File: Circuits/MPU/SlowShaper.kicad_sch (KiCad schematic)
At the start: 34 parts, among them U22 ADA4805-2ARMZ, U23 ADA4805-2ARMZ

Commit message: revert cap changes from sim. Don't trust it...
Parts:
- C98: value 3.9nF -> 3.3nF
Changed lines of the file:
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@@
 			)
 		)
-		(property "Value" "3.9nF"
+		(property "Value" "3.3nF"
 			(at 149.86 102.87 90)
 			(effects

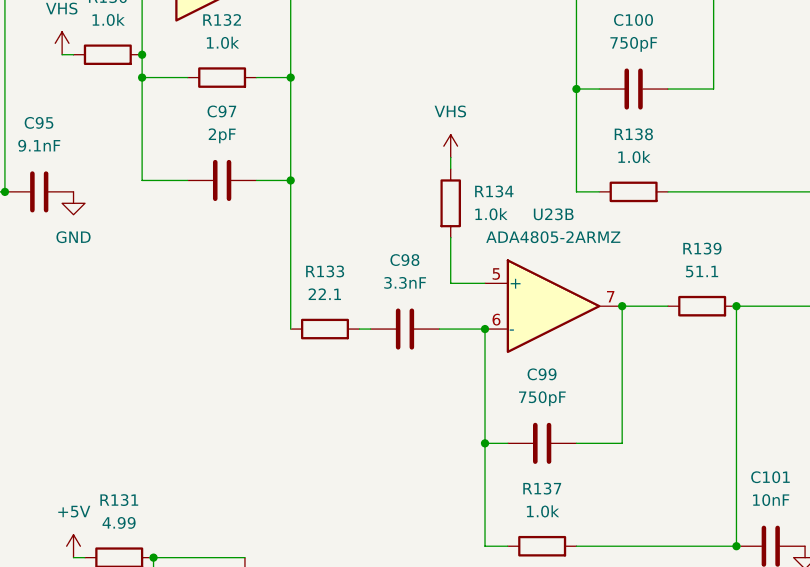
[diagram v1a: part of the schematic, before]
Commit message: tweak shaper caps based on sim
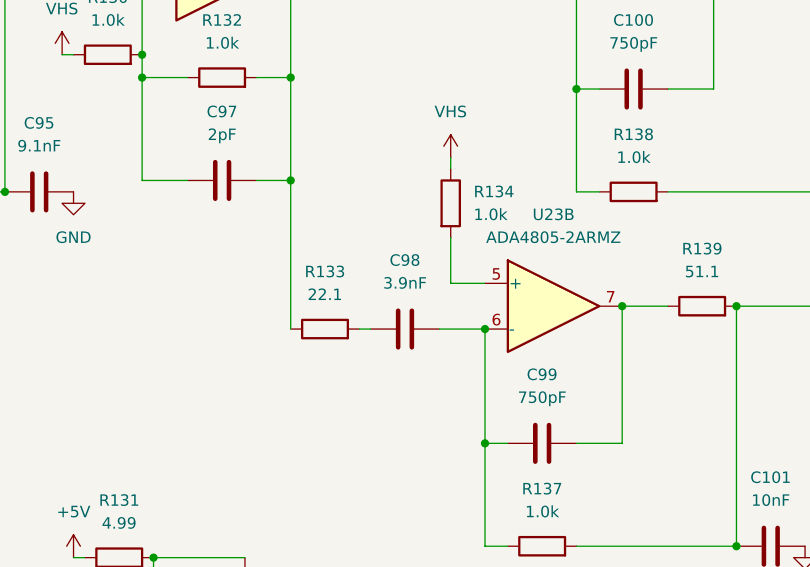
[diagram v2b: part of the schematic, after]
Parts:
- C98: value 3.3nF -> 3.9nF
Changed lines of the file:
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@@
 			)
 		)
-		(property "Value" "3.3nF"
+		(property "Value" "3.9nF"
 			(at 149.86 102.87 90)
 			(effects
